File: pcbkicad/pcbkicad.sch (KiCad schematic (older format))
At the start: 38 parts, among them J1 USBDaughterboard, U1 AMS1117-3.3, U2 STM32F072CBTx

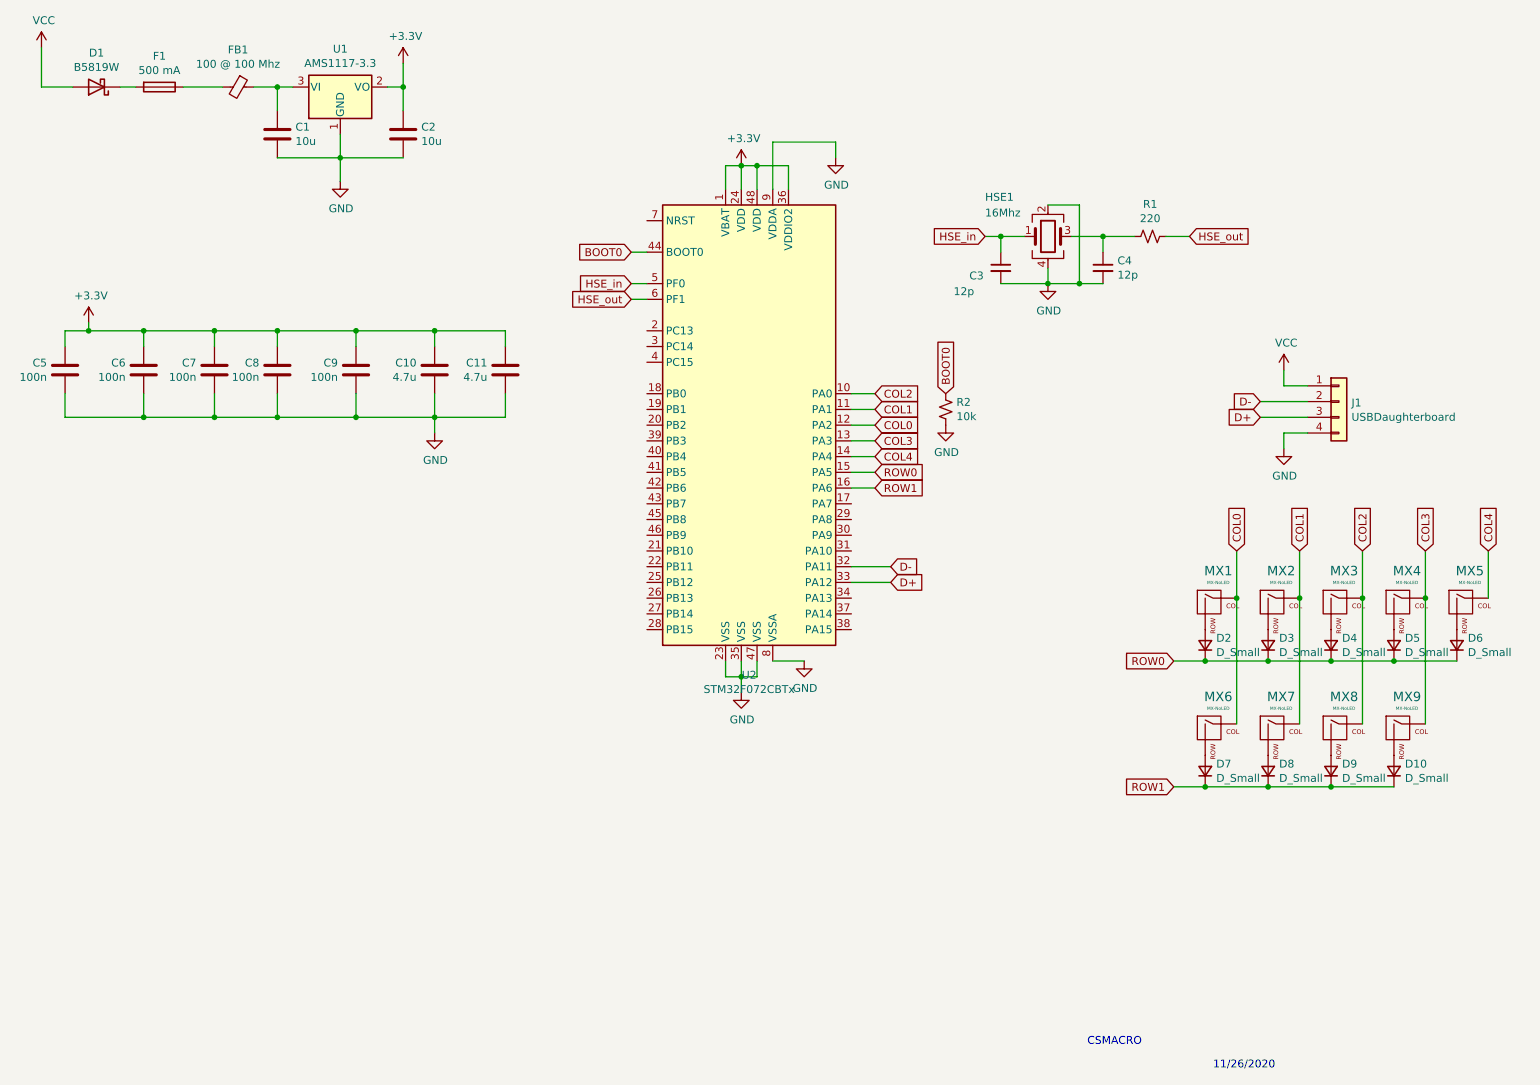
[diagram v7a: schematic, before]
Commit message: Rerouted and removed unecessary elements
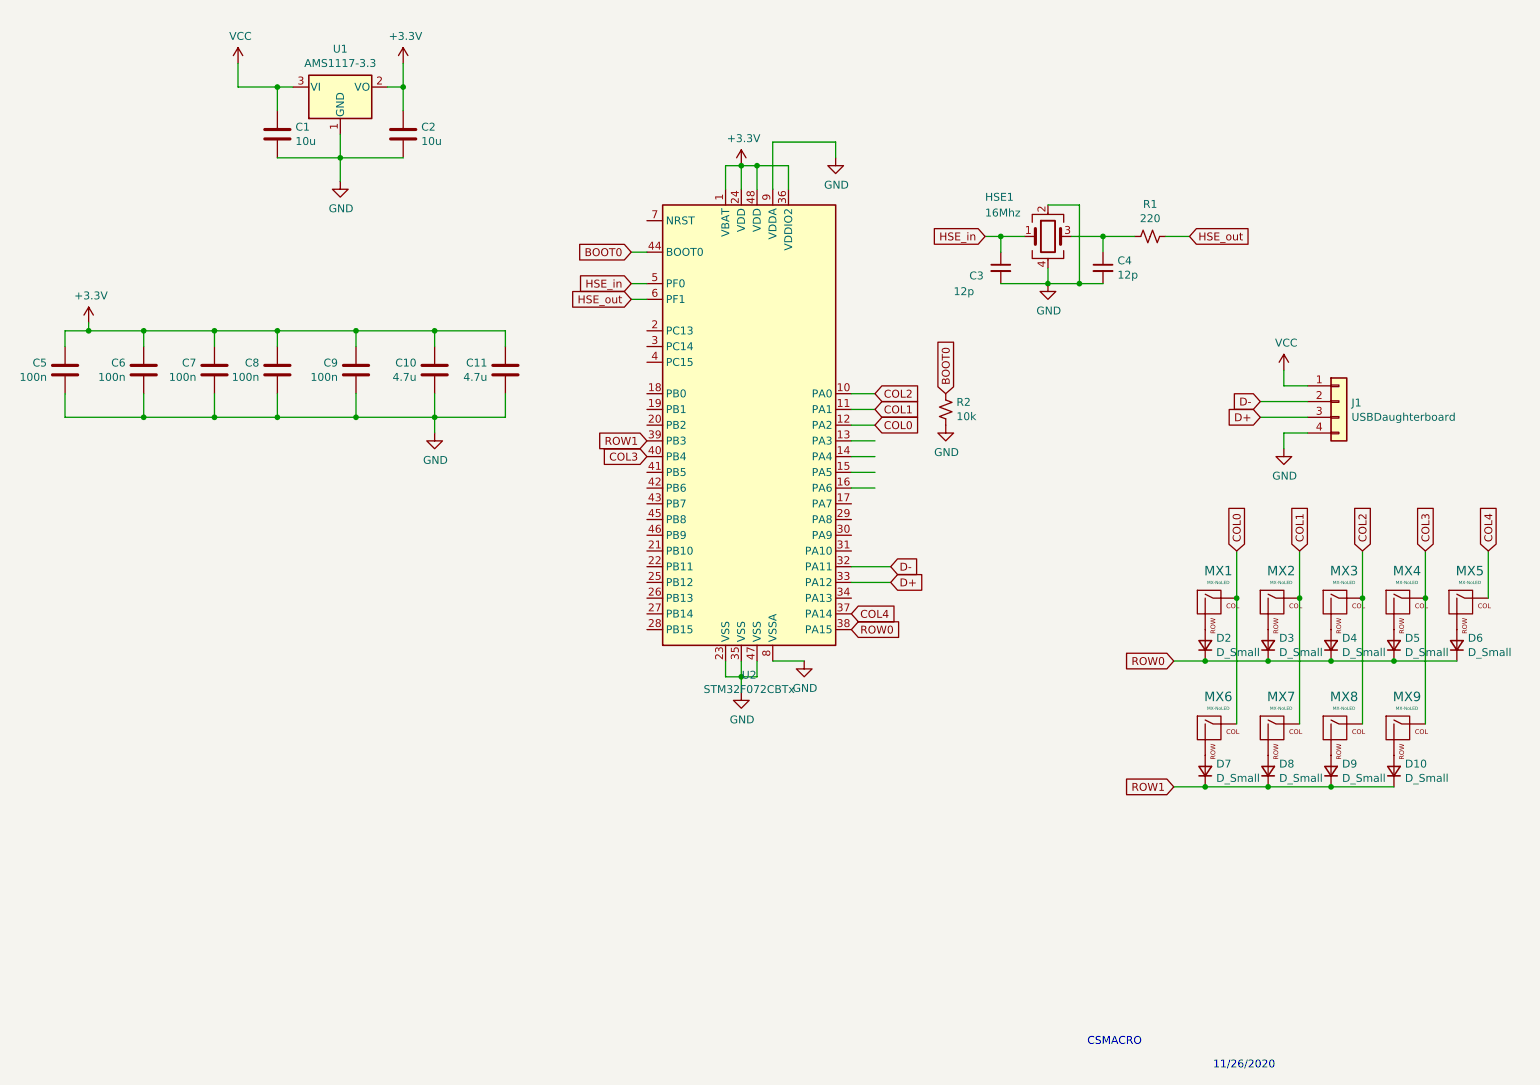
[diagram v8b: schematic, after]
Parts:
- removed D1: B5819W, Diode_SMD:D_SOD-123, symbol Device:D_Schottky
- removed F1: 500 mA, Fuse:Fuse_1206_3216Metric, symbol Device:Fuse
- removed FB1: 100 @ 100 Mhz, Ferrite_THT:LairdTech_28C0236-0JW-10, symbol Device:Ferrite_Bead_Small
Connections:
- wire segments 109 -> 106
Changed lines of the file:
@@
-$EndComp
-$Comp
-L Device:Ferrite_Bead_Small FB1
-U 1 1 5FC0D8E0
-P 1950 1400
-F 0 "FB1" V 1713 1400 50  0000 C CNN
-F 1 "100 @ 100 Mhz" V 1804 1400 50  0000 C CNN
-F 2 "Ferrite_THT:LairdTech_28C0236-0JW-10" V 1880 1400 50  0001 C CNN
-F 3 "~" H 1950 1400 50  0001 C CNN
-	1    1950 1400
-	0    1    1    0
-$EndComp
-$Comp
-L Device:Fuse F1
-U 1 1 5FC12F50
-P 1450 1400
-F 0 "F1" V 1253 1400 50  0000 C CNN
-F 1 "500 mA" V 1344 1400 50  0000 C CNN
-F 2 "Fuse:Fuse_1206_3216Metric" V 1380 1400 50  0001 C CNN
-F 3 "~" H 1450 1400 50  0001 C CNN
-	1    1450 1400
-	0    1    1    0
-$EndComp
-$Comp
-L Device:D_Schottky D1
-U 1 1 5FC1706D
-P 1050 1400
-F 0 "D1" H 1050 1183 50  0000 C CNN
-F 1 "B5819W" H 1050 1274 50  0000 C CNN
-F 2 "Diode_SMD:D_SOD-123" H 1050 1400 50  0001 C CNN
-F 3 "~" H 1050 1400 50  0001 C CNN
-	1    1050 1400
-	-1   0    0    1
 $EndComp
 $Comp
@@
 Wire Wire Line
 	2300 1400 2200 1400
-Wire Wire Line
-	1850 1400 1600 1400
-Wire Wire Line
-	1300 1400 1200 1400
-$Comp
-L power:VCC #PWR0101
-U 1 1 5FC2288E
-P 700 1150
-F 0 "#PWR0101" H 700 1000 50  0001 C CNN
-F 1 "VCC" H 715 1323 50  0000 C CNN
-F 2 "" H 700 1150 50  0001 C CNN
-F 3 "" H 700 1150 50  0001 C CNN
-	1    700  1150
-	1    0    0    -1
-$EndComp
-Wire Wire Line
-	700  1150 700  1400
-Wire Wire Line
-	700  1400 900  1400
 $Comp
 L power:GND #PWR0102
@@
 Wire Wire Line
 	2200 1550 2200 1400
-Connection ~ 2200 1400
-Wire Wire Line
-	2200 1400 2050 1400
 Wire Wire Line
 	3000 1550 3000 1400
@@
 Text GLabel 6000 3350 2    50   Input ~ 0
 COL2
-Text GLabel 6000 3650 2    50   Input ~ 0
+Text GLabel 4550 3750 0    50   Input ~ 0
 COL3
-Text GLabel 6000 3750 2    50   Input ~ 0
+Text GLabel 5850 4750 2    50   Input ~ 0
 COL4
-Text GLabel 6000 3850 2    50   Input ~ 0
+Text GLabel 5850 4850 2    50   Input ~ 0
 ROW0
-Text GLabel 6000 3950 2    50   Input ~ 0
+Text GLabel 4550 3650 0    50   Input ~ 0
 ROW1
 Wire Wire Line
@@
 Wire Wire Line
 	6000 3450 5850 3450
+$Comp
+L power:VCC #PWR0101
+U 1 1 5FC3DB8A
+P 1950 1250
+F 0 "#PWR0101" H 1950 1100 50  0001 C CNN
+F 1 "VCC" H 1965 1423 50  0000 C CNN
+F 2 "" H 1950 1250 50  0001 C CNN
+F 3 "" H 1950 1250 50  0001 C CNN
+	1    1950 1250
+	1    0    0    -1
+$EndComp
+Wire Wire Line
+	1950 1250 1950 1400
+Wire Wire Line
+	1950 1400 2200 1400
+Connection ~ 2200 1400
 $EndSCHEMATC
